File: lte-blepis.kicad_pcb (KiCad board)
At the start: 2 copper layers, 24.1 x 60.6 mm, 75 parts, among them J1 MODEM_USB, J53 EXP, Q1 NPN, Q2 NPN, Q3 NPN, Q4 NPN, SW1 EVQPUL02K, SW2 EVQPUL02K, SW3 EVQPUL02K, U1 A7682E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

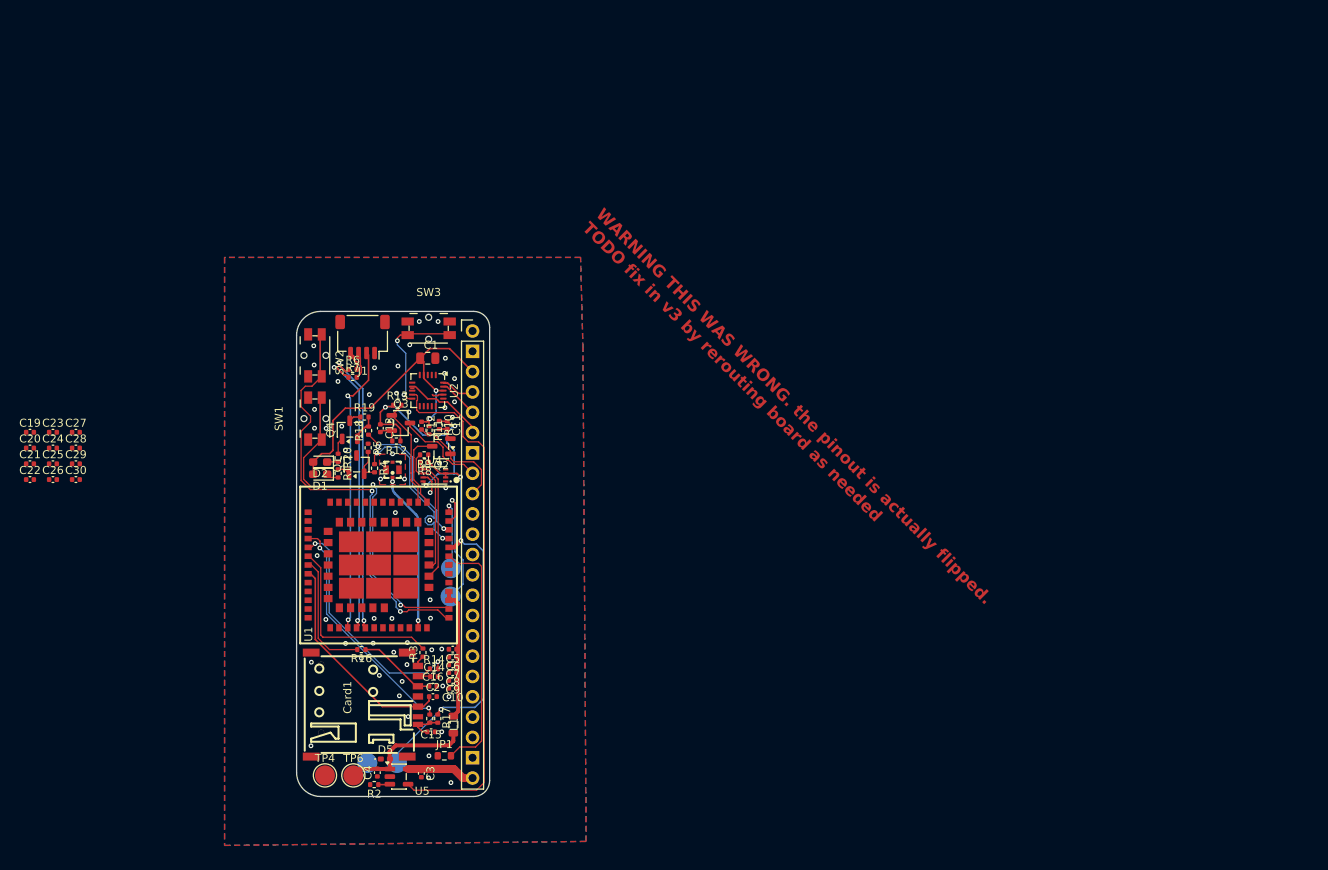
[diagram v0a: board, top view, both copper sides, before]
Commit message: refactor: flip design, flip footprints, re-do routing
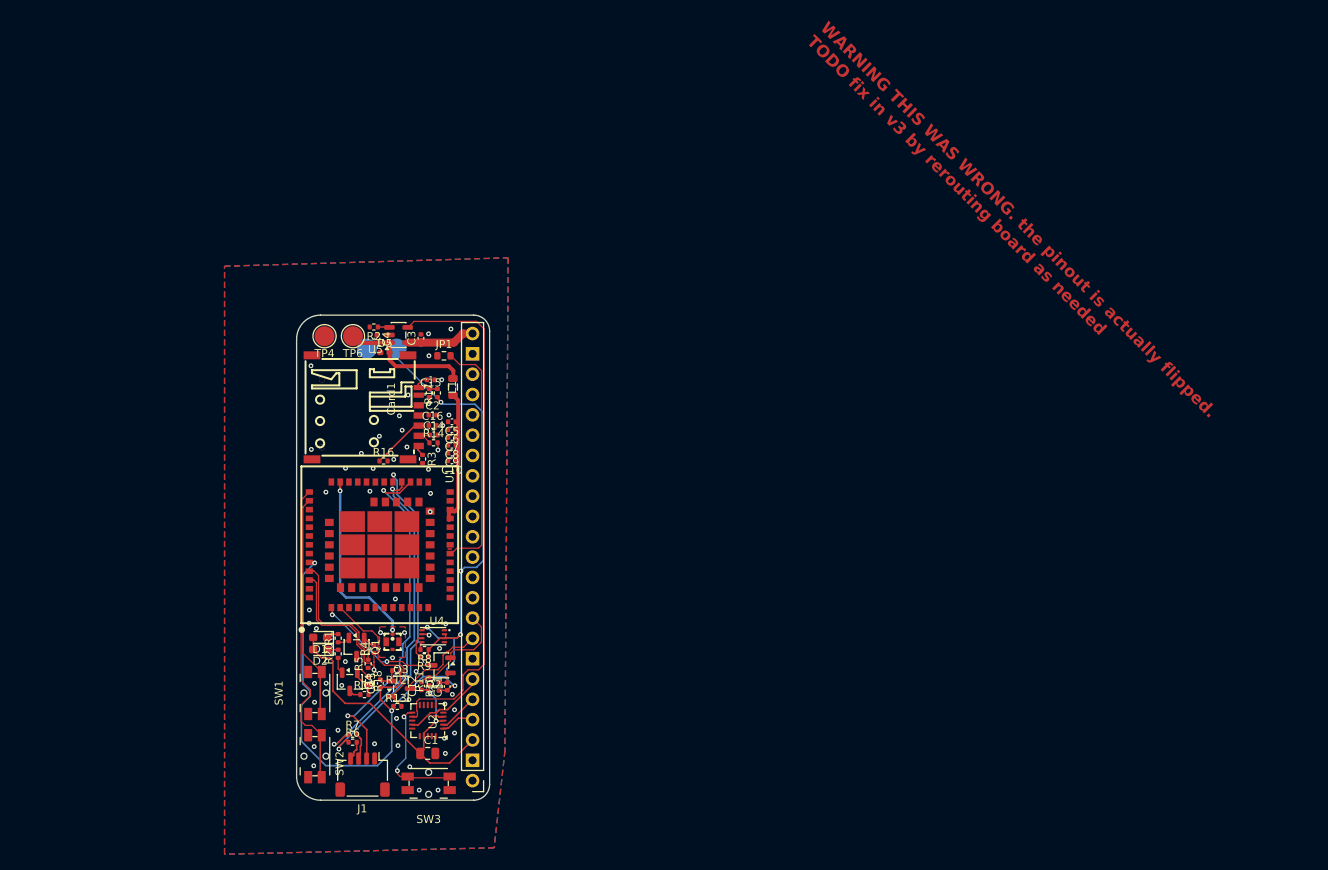
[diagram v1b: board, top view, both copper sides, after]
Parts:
- removed C19, C21, C23, C25, C26, C27: 100p, Capacitor_SMD:C_0402_1005Metric
- removed C20, C22, C24, C28, C29, C30: 33p, Capacitor_SMD:C_0402_1005Metric
- removed G***: LOGO, LOGO
- removed TP1, TP2: TestPoint, TestPoint:TestPoint_Pad_D2.5mm
- moved R2 57.2 mm to (186.7, 53.7)
- moved SW3 56.9 mm to (193.5, 110.7), turned to 180 degrees
- moved J53 56.2 mm to (199.0, 110.4), turned to 180 degrees
- moved U5 55.2 mm to (189.8, 54.7), turned to 180 degrees
- moved TP4 54.9 mm to (180.5, 54.9), turned to 180 degrees
- moved TP6 54.9 mm to (184.1, 54.9), turned to 180 degrees
- moved J1 54.7 mm to (185.2, 109.7), turned to 0 degrees
- moved C3 54.4 mm to (192.6, 55.1), turned to 90 degrees
- moved C4 54.2 mm to (187.1, 55.2), turned to 90 degrees
- moved TP3 51.8 mm to (185.8, 56.4), turned to 0 degrees
- moved TP5 51.8 mm to (189.5, 56.4), turned to 0 degrees
- moved D5 50.8 mm to (188.1, 56.9)
- moved SW2 50.1 mm to (179.3, 107.3)
- moved JP1 50.0 mm to (195.4, 57.3)
- moved C1 49.4 mm to (193.4, 107.0)
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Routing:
- net VDD_EXT: track 84.7 -> 126.8 mm, vias 6 -> 7
- net Net-(U1-SIM1_DET): track 29.6 -> 0.87 mm, vias 2 -> 1
- net Net-(U1-SIM1_DATA): track 29.2 -> 0.90 mm, vias 2 -> 1
- net /SIM1_VDD: track 27.3 -> 0.00 mm
- net Net-(U1-SIM1_CLK): track 24.1 -> 0.00 mm
- net /DBG_RXD: track 16.4 -> 0.00 mm, vias 1 -> 0
- net /MODEM_RST: track 43.3 -> 27.9 mm, vias 2 -> 0
- net /MODEM_SDA: track 16.1 -> 0.99 mm
- net Net-(U1-SIM1_RST): track 15.4 -> 0.40 mm
- net /BOOT_CFG: track 53.7 -> 38.8 mm, vias 2 -> 0
- net /MODEM_SCL: track 16.3 -> 3.20 mm
- net /DBG_TXD: track 8.83 -> 0.00 mm, vias 1 -> 0
- net /USB_VBUS: track 36.2 -> 44.0 mm
- net /UART1_TXD: track 9.17 -> 16.1 mm, vias 0 -> 2
- net /MODEM_USB_DN: track 36.6 -> 42.5 mm
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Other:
- board text removed: "hackmods moment"

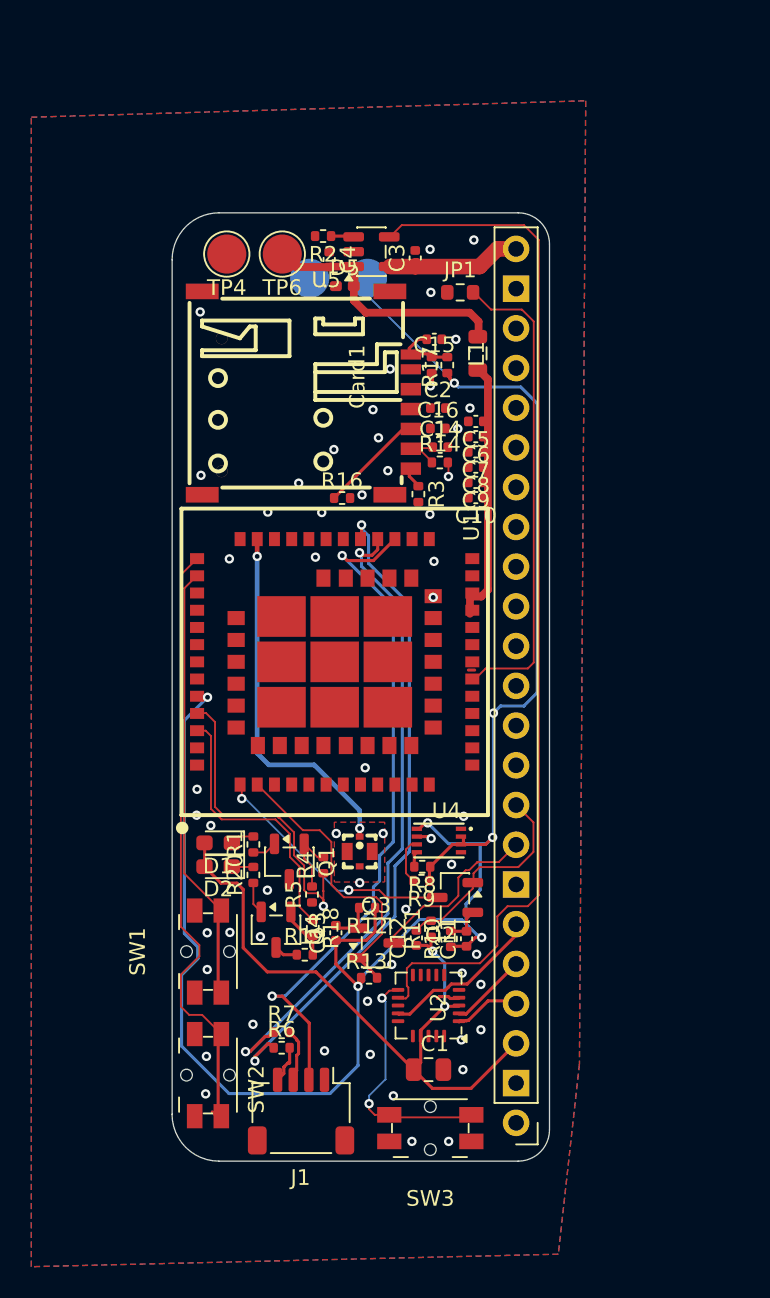
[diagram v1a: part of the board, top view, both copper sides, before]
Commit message: flip sd card footprint to correct orientation, re-do wiring
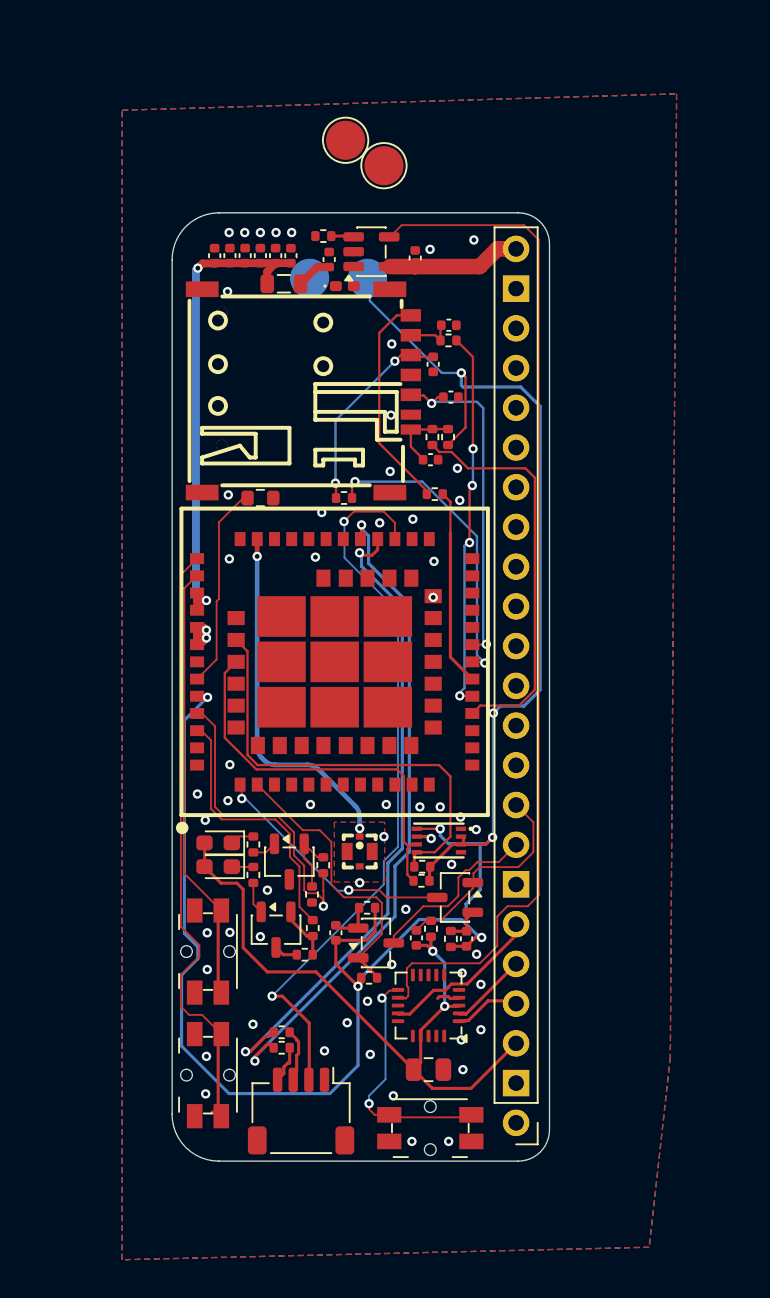
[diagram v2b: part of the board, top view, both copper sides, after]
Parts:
- moved C10 22.8 mm to (179.7, 55.0), turned to 90 degrees
- moved C9 21.4 mm to (180.7, 55.0), turned to 90 degrees
- moved C8 20.0 mm to (181.7, 55.0), turned to 90 degrees
- moved C7 18.6 mm to (182.7, 55.0), turned to 90 degrees
- moved JP1 18.3 mm to (182.7, 70.5), turned to 180 degrees
- moved C6 17.3 mm to (183.6, 55.0), turned to 90 degrees
- moved C5 15.9 mm to (184.6, 55.0), turned to 90 degrees
- moved L1 13.2 mm to (184.2, 56.8), turned to 180 degrees
- moved TP4 11.5 mm to (190.6, 49.2)
- moved TP6 8.33 mm to (188.1, 47.6)
- moved C14 7.82 mm to (194.7, 59.4)
- moved R14 7.82 mm to (194.7, 60.4)
- moved C15 7.70 mm to (193.5, 68.0)
- moved R15 4.60 mm to (193.7, 66.5)
- moved R17 4.60 mm to (194.7, 66.5)
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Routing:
- net /MODEM_SDA: track 0.99 -> 28.6 mm
- net Net-(U1-SIM1_DET): track 0.87 -> 25.6 mm, vias 1 -> 0
- net Net-(U1-SIM1_DATA): track 0.90 -> 24.4 mm, vias 1 -> 4
- net /SIM1_VDD: track 0.00 -> 22.1 mm, vias 0 -> 2
- net /MODEM_SCL: track 3.20 -> 25.2 mm
- net Net-(U1-SIM1_RST): track 0.40 -> 19.5 mm, vias 0 -> 2
- net Net-(JP1-B): track 31.0 -> 13.1 mm
- net Net-(C10-Pad1): track 16.7 -> 31.1 mm, vias 0 -> 2
- net /MODEM_VBAT: track 16.6 -> 2.28 mm
- net Net-(U1-SIM1_CLK): track 0.00 -> 12.7 mm
- net /SIM1_CLK: track 1.42 -> 14.1 mm
- net /SIM1_RST: track 6.74 -> 13.0 mm, vias 0 -> 2
- net VDD_EXT: track 126.8 -> 132.0 mm
- net GND: track 3.80 -> 7.05 mm, vias 54 -> 60
- net /USB_VBUS: track 44.0 -> 46.7 mm

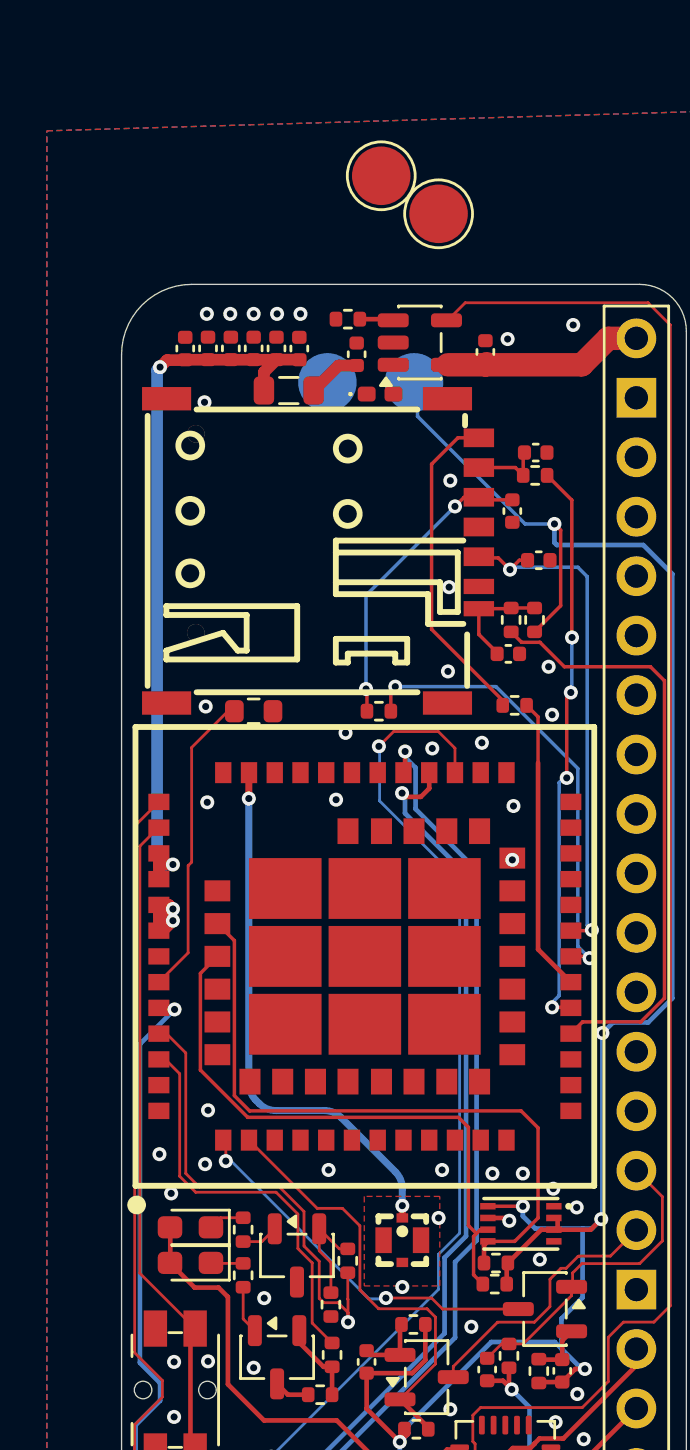
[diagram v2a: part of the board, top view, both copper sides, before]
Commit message: tidy up test points and traces
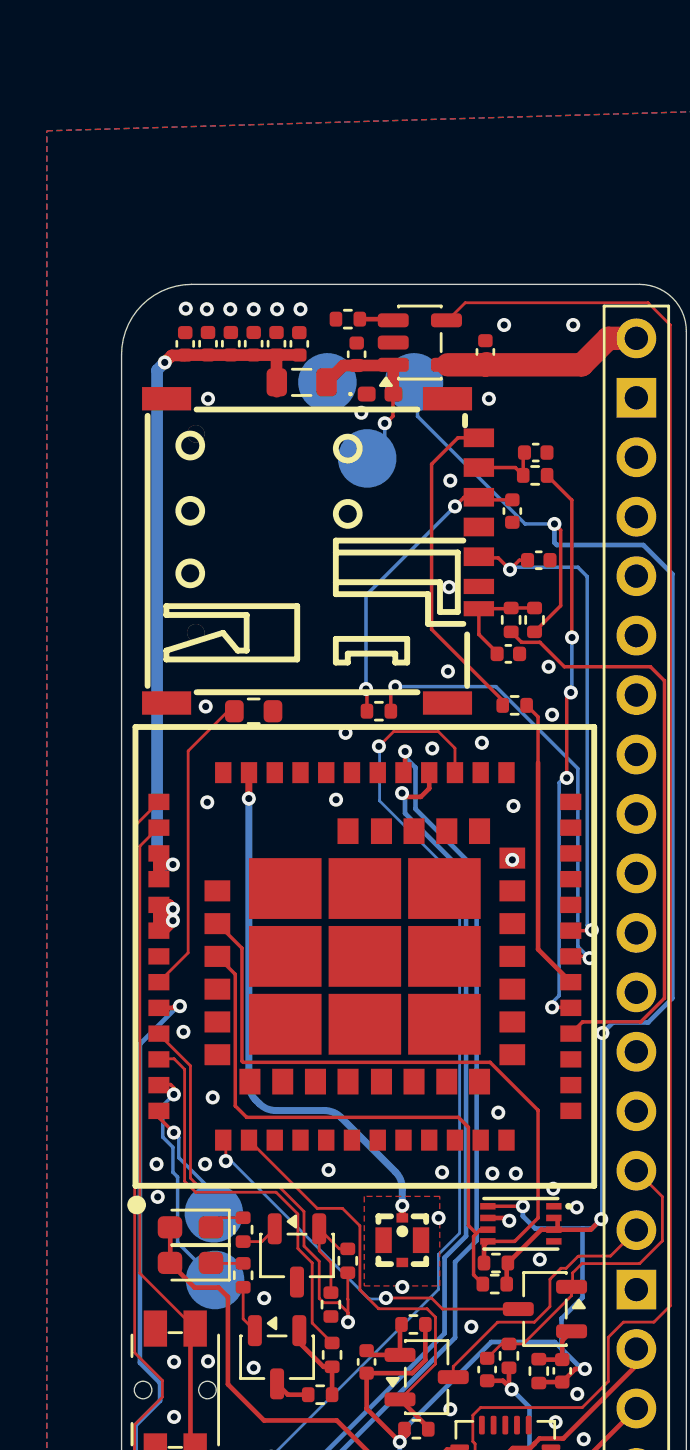
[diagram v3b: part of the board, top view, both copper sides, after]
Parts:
- removed TP4: TestPoint, TestPoint:TestPoint_Pad_D2.5mm
- added TP1: TestPoint, TestPoint:TestPoint_Pad_D2.5mm, B.Cu at (180.9, 91.9)
- added TP2: TestPoint, TestPoint:TestPoint_Pad_D2.5mm, B.Cu at (181.0, 94.8)
- TP6: moved to B.Cu
- moved TP6 12.1 mm to (187.5, 59.6), turned to 0 degrees
- moved L1 0.65 mm to (184.7, 56.4)
- moved C6 0.20 mm to (183.6, 54.8)
- moved C7 0.20 mm to (182.7, 54.8)
- moved C8 0.20 mm to (181.7, 54.8)
- moved C9 0.20 mm to (180.7, 54.8)
- moved C10 0.20 mm to (179.7, 54.8)
- moved C5 0.20 mm to (184.6, 54.8)
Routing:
- net /DBG_RXD: track 0.00 -> 10.0 mm, vias 0 -> 1
- net /MODEM_VBAT: track 2.28 -> 7.66 mm, vias 0 -> 1
- net /DBG_TXD: track 0.00 -> 5.35 mm, vias 0 -> 1
- net /MODEM_SDA: track 28.6 -> 28.0 mm
- net /MODEM_SCL: track 25.2 -> 24.7 mm
- net VDD_EXT: track 132.0 -> 132.5 mm
- net GND: vias 60 -> 65
